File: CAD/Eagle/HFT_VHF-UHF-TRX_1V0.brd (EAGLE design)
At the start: 70 x 80 mm, 123 parts, among them IC1 AX5243, IC2 AX5243, IC3 AX5243, IC4 AX5243, IC5 ICS552A-01, J1 SMA_SMT_AMPHENOL-901-143, J2 SMA_SMT_AMPHENOL-901-143, J3 SMA_SMT_AMPHENOL-901-143, J4 SMA_SMT_AMPHENOL-901-143, Q2 ABM03B-16.000MHZ

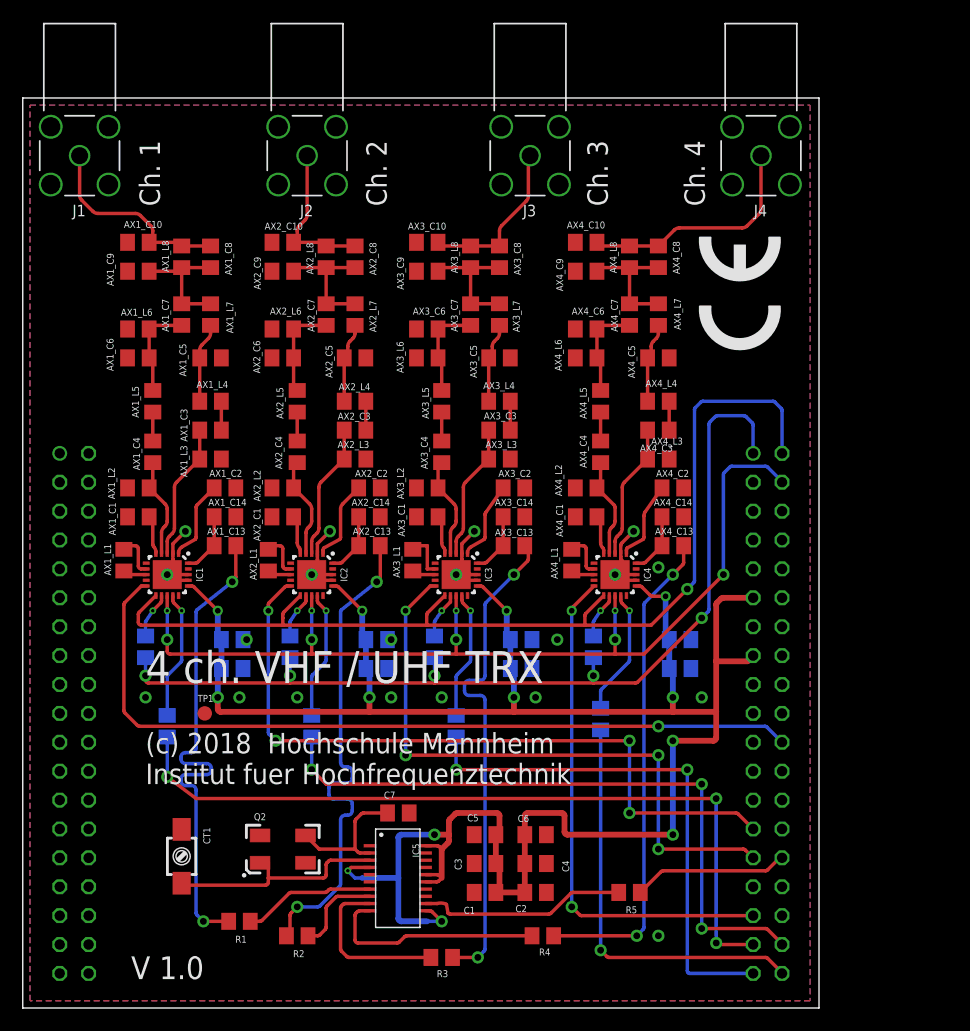
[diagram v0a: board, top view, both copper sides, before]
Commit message: HW_1V0 - revert board to un-modified version - make lines at least with 0.1mm width
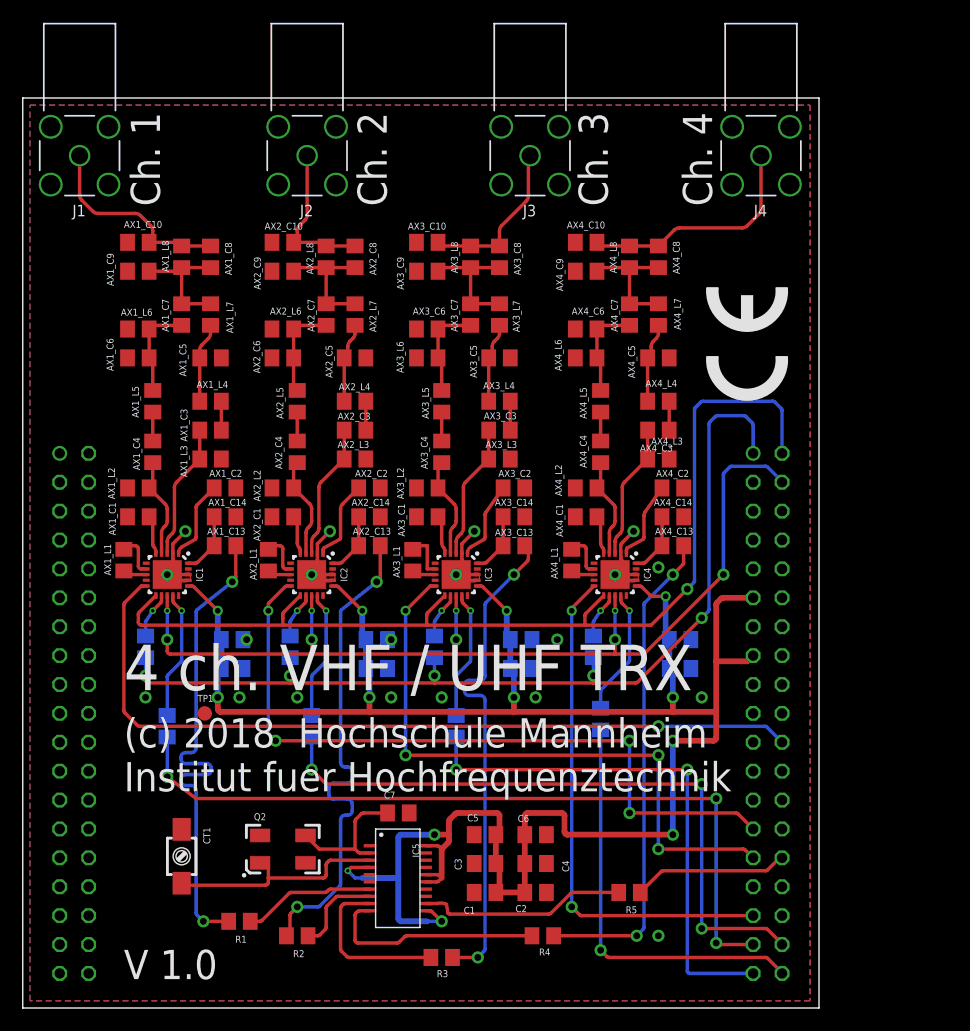
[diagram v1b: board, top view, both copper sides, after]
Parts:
- moved X_CE_LOGO 4.49 mm to (67.3, 53.3)
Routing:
- added copper zone on layer 1, net N$2
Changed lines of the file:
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@@
 <layer number="37" name="tTest" color="7" fill="1" visible="no" active="yes"/>
 <layer number="38" name="bTest" color="7" fill="1" visible="no" active="yes"/>
-<layer number="39" name="tKeepout" color="4" fill="11" visible="yes" active="yes"/>
-<layer number="40" name="bKeepout" color="1" fill="11" visible="yes" active="yes"/>
-<layer number="41" name="tRestrict" color="4" fill="10" visible="yes" active="yes"/>
+<layer number="39" name="tKeepout" color="4" fill="11" visible="no" active="yes"/>
+<layer number="40" name="bKeepout" color="1" fill="11" visible="no" active="yes"/>
+<layer number="41" name="tRestrict" color="4" fill="10" visible="no" active="yes"/>
 <layer number="42" name="bRestrict" color="1" fill="10" visible="no" active="yes"/>
 <layer number="43" name="vRestrict" color="2" fill="10" visible="no" active="yes"/>
@@
 <dimension x1="0" y1="0" x2="0" y2="80" x3="-10.16" y3="40" textsize="1.778" layer="47"/>
 <dimension x1="0" y1="0" x2="70" y2="0" x3="35" y3="-8.89" textsize="1.778" layer="47"/>
-<text x="10.795" y="28.575" size="2.8" layer="21">4 ch. VHF / UHF TRX</text>
-<text x="10.795" y="19.685" size="1.8" layer="21" ratio="10">(c) 2018  Hochschule Mannheim
+<text x="8.89" y="27.94" size="4" layer="21">4 ch. VHF / UHF TRX</text>
+<text x="8.89" y="19.05" size="2.57" layer="21">(c) 2018  Hochschule Mannheim
 Institut fuer Hochfrequenztechnik</text>
-<text x="9.525" y="2.54" size="2" layer="21" ratio="10">V 1.0</text>
-<text x="12.065" y="70.485" size="1.8" layer="21" rot="R90">Ch. 1</text>
-<text x="32" y="70.485" size="1.8" layer="21" rot="R90">Ch. 2</text>
-<text x="51.435" y="70.485" size="1.8" layer="21" rot="R90">Ch. 3</text>
-<text x="59.965" y="70.485" size="1.8" layer="21" rot="R90">Ch. 4</text>
-<rectangle x1="53.34" y1="37.465" x2="53.8" y2="38.1" layer="41"/>
-<rectangle x1="39.37" y1="37.465" x2="39.83" y2="38.1" layer="41"/>
-<rectangle x1="26.67" y1="37.465" x2="27.13" y2="38.1" layer="41"/>
-<rectangle x1="13.97" y1="37.465" x2="14.43" y2="38.1" layer="41"/>
+<text x="8.89" y="2.54" size="2.57" layer="21">V 1.0</text>
+<text x="12.065" y="70.485" size="2.57" layer="21" rot="R90">Ch. 1</text>
+<text x="32" y="70.485" size="2.57" layer="21" rot="R90">Ch. 2</text>
+<text x="51.435" y="70.485" size="2.57" layer="21" rot="R90">Ch. 3</text>
+<text x="60.6" y="70.485" size="2.57" layer="21" rot="R90">Ch. 4</text>
 </plain>
 <attributes>
@@
 <attribute name="VALUE" x="15.365" y="25.138" size="0.0254" layer="27"/>
 </element>
-<element name="X_CE_LOGO" library="logo" package="CE_7.3MM" value="" x="66.675" y="57.785" rot="R90"/>
+<element name="X_CE_LOGO" library="logo" package="CE_7.3MM" value="" x="67.31" y="53.34" rot="R90"/>
 </elements>
 <signals>
@@
 <via x="59.69" y="27.305" extent="1-16" drill="0.6"/>
 </signal>
+<signal name="N$2">
+<polygon width="0.05" layer="1" spacing="0.254" pour="cutout" isolate="0.254">
+<vertex x="54.11" y="38.235"/>
+<vertex x="53.305" y="38.235"/>
+<vertex x="53.305" y="37.465"/>
+<vertex x="54.11" y="37.465"/>
+</polygon>
+<polygon width="0.05" layer="1" spacing="0.254" pour="cutout" isolate="0.254">
+<vertex x="40.14" y="38.235"/>
+<vertex x="39.335" y="38.235"/>
+<vertex x="39.335" y="37.465"/>
+<vertex x="40.14" y="37.465"/>
+</polygon>
+<polygon width="0.05" layer="1" spacing="0.254" pour="cutout" isolate="0.254">
+<vertex x="27.44" y="38.235"/>
+<vertex x="26.635" y="38.235"/>
+<vertex x="26.635" y="37.465"/>
+<vertex x="27.44" y="37.465"/>
+</polygon>
+<polygon width="0.05" layer="1" spacing="0.254" pour="cutout" isolate="0.254">
+<vertex x="14.74" y="38.235"/>
+<vertex x="13.935" y="38.235"/>
+<vertex x="13.935" y="37.465"/>
+<vertex x="14.74" y="37.465"/>
+</polygon>
+</signal>
 </signals>
